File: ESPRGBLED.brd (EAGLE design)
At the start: 22.5 x 25.7 mm, 25 parts

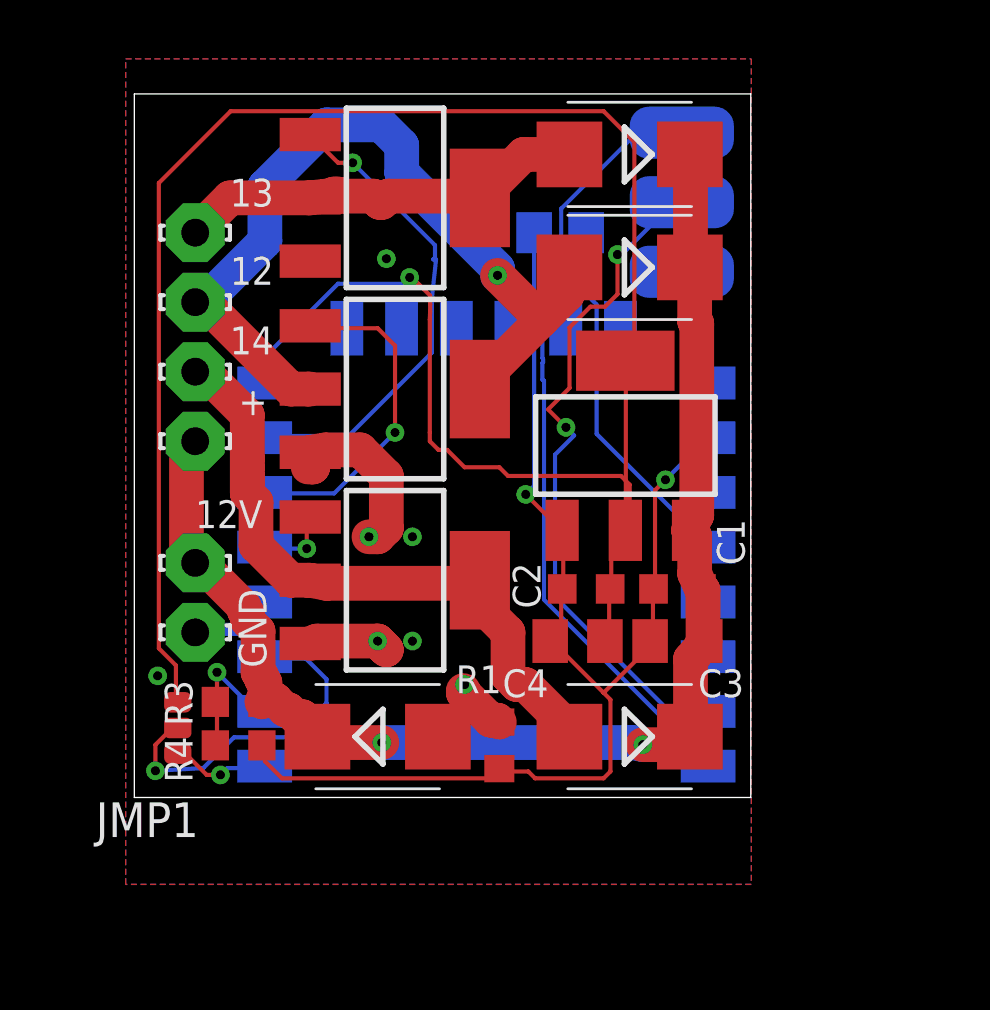
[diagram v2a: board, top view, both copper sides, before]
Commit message: updated schematics with step down vreg
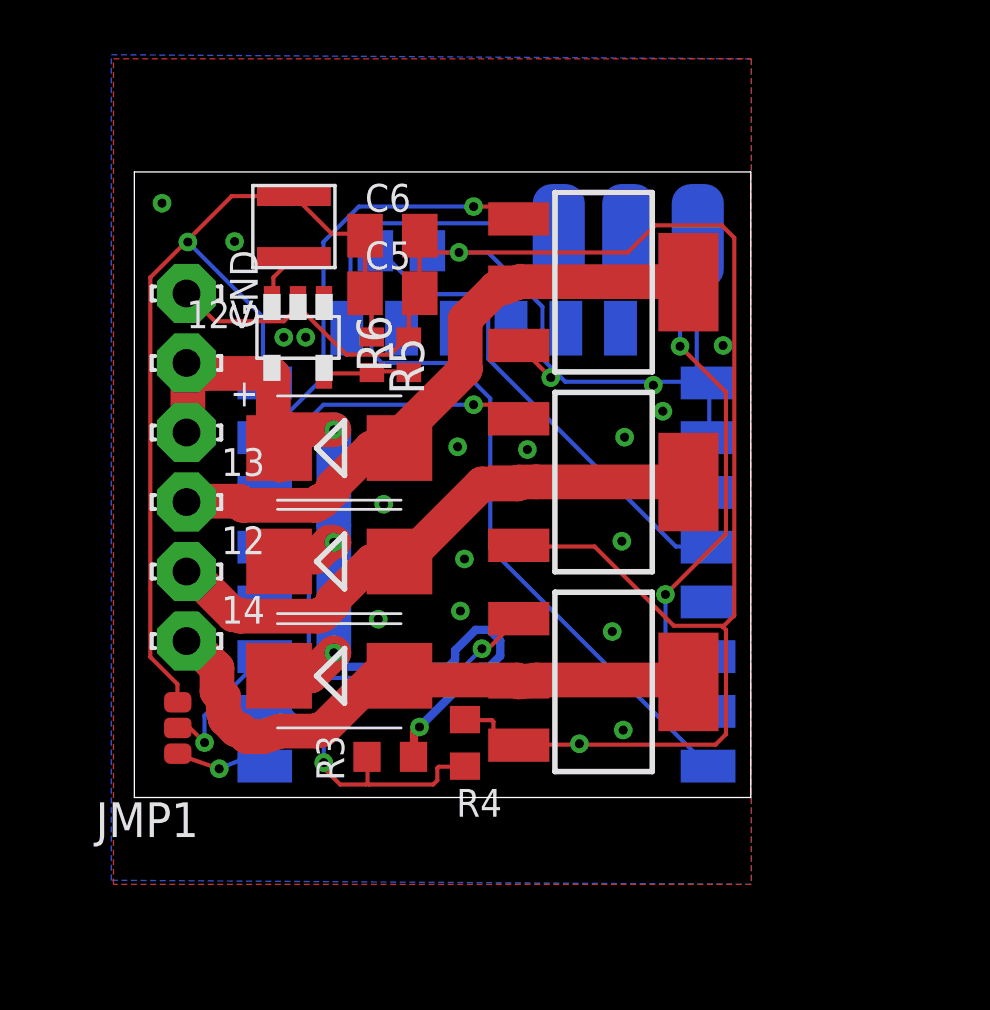
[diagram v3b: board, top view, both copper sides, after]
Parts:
- removed C1, C2: (no value), rcl:C0603K
- removed C3, C4: (no value), rcl:C0805K
- removed D1: MBRS130LT3, diode:SMB
- removed R1: 0R, rcl:R0603
- removed U$1: LM1117, Fabian:SOT223
- added C5, C6: 10uF, rcl:C0805K
- added L1: L_10UH_560MA, Fabian:TYS3010100M-10
- added R5, R6: (no value), rcl:R0402
- added U$2: TPS560200, Fabian:SOT23-5
- moved PWR2:D1 15.1 mm to (6.22, 11.8), turned to 0 degrees
- moved PWR1:D1 15.1 mm to (6.22, 15.9), turned to 0 degrees
- moved GND 12.4 mm to (0.64, 21.6)
- moved PWR3:D1 10.8 mm to (6.22, 7.62), turned to 0 degrees
- moved 12 9.85 mm to (0.64, 11.4)
- moved 14 9.85 mm to (0.64, 8.89)
- moved 13 9.85 mm to (0.64, 14.0)
- moved PWR3:T1 8.48 mm to (15.9, 7.40)
- moved PWR2:T1 8.34 mm to (15.9, 14.7)
- moved R4 8.27 mm to (10.8, 5.17), turned to 270 degrees
- moved PWR1:T1 8.22 mm to (15.9, 22.0)
- moved 12V 7.31 mm to (0.64, 19.1)
- moved R3 5.89 mm to (8.08, 4.66)
- moved R2 5.84 mm to (8.49, 23.2), turned to 180 degrees
- moved U$3 2.32 mm to (16.8, 23.7), turned to 0 degrees
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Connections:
- removed net DGND: C1.2, C2.2, C3.2, C4.2, MDL1.10, MDL1.9, R1.1, R2.2, R4.1, U$1.LEFT, U$3.0V
- new net N$13: L1.P$1, U$2.3
- new net N$15: R5.2, R6.1, U$2.5
- net +12V: now also U$2.4; no longer C1.1, C3.1, D1.C, U$1.RIGHT
- net GND: now also C5.2, C6.2, MDL1.10, MDL1.9, R2.2, R4.1, R6.2, U$2.2, U$3.0V; no longer D1.A, R1.2
- net VCC: now also C5.1, C6.1, L1.P$2, R5.1; no longer C2.1, C4.1, U$1.MID, U$1.TAP
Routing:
- net GND: track 12.9 -> 87.7 mm, vias 7 -> 20
- net DGND: track 55.5 -> 0.00 mm, vias 2 -> 0
- net VCC: track 80.4 -> 35.8 mm
- net +12V: track 49.1 -> 37.5 mm, vias 2 -> 4
- net N$2: track 2.80 -> 13.7 mm
- net N$4: track 31.6 -> 21.1 mm, vias 1 -> 0
- net N$1: track 15.1 -> 23.2 mm
- net N$12: track 12.8 -> 5.27 mm
- net N$10: track 5.07 -> 10.5 mm
- net N$8: track 25.8 -> 20.4 mm
- net N$7: track 29.3 -> 34.5 mm
- net N$9: track 13.4 -> 17.8 mm
- net N$15: track 0.00 -> 3.16 mm
- net N$5: track 23.9 -> 21.8 mm
- net N$13: track 0.00 -> 1.93 mm
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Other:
- board size 22.5 x 25.7 mm -> 22.5 x 22.9 mm

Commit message: layout stuff
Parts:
- moved JMP1 23.2 mm to (23.2, 2.02), turned to 270 degrees
- moved C6 20.6 mm to (11.0, 3.27), turned to 270 degrees
- moved MDL1 18.8 mm to (8.17, 2.12), turned to 90 degrees
- moved L1 18.5 mm to (11.3, 6.87), turned to 0 degrees
- moved C5 18.3 mm to (8.90, 3.27), turned to 270 degrees
- moved R6 16.5 mm to (6.70, 3.02), turned to 0 degrees
- moved GND 15.3 mm to (1.91, 6.35)
- moved R5 15.0 mm to (6.70, 4.32), turned to 180 degrees
- moved U$2 13.5 mm to (7.29, 6.72), turned to 90 degrees
- moved 12V 10.2 mm to (1.91, 8.89)
- moved R4 9.01 mm to (1.95, 3.54)
- moved PWR1:D1 5.68 mm to (8.76, 21.0)
- moved + 5.24 mm to (1.91, 11.4)
- moved 12 5.24 mm to (1.91, 16.5)
- moved 13 5.24 mm to (1.91, 19.1)
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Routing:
- net N$7: track 34.5 -> 3.56 mm
- net N$10: track 10.5 -> 32.0 mm, vias 1 -> 3
- net N$8: track 20.4 -> 3.81 mm, vias 2 -> 0
- net GND: track 87.7 -> 99.1 mm
- net +12V: track 37.5 -> 27.6 mm, vias 4 -> 2
- net N$6: track 15.9 -> 23.4 mm, vias 1 -> 3
- net N$2: track 13.7 -> 6.22 mm
- net N$5: track 21.8 -> 28.3 mm, vias 0 -> 1
- net N$9: track 17.8 -> 12.5 mm
- net VCC: track 35.8 -> 32.0 mm, vias 1 -> 2
- net N$3: track 11.5 -> 14.1 mm
- net N$4: track 21.1 -> 23.4 mm, vias 0 -> 1
- net N$15: track 3.16 -> 3.89 mm
- net N$1: track 23.2 -> 22.5 mm
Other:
- board size 22.5 x 22.9 mm -> 25.2 x 24.1 mm

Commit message: superminiaturized
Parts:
- added C1, C2: 10uF, rcl:C0805K
- added R1: 0R, rcl:R0402
- R5: value (none) -> 61k9
- R6: value (none) -> 20k
- moved U$3 25.8 mm to (4.12, 2.40), turned to 0 degrees
- moved MDL1 22.0 mm to (17.1, 22.2), turned to 270 degrees
- moved JMP1 20.6 mm to (19.1, 22.2), flipped to the bottom
- moved R2 20.5 mm to (11.0, 2.71), turned to 180 degrees
- moved C6 20.2 mm to (2.54, 21.6), turned to 0 degrees
- moved + 17.8 mm to (19.7, 11.7)
- moved 12 17.8 mm to (19.7, 16.8)
- moved 12V 17.8 mm to (19.7, 9.21)
- moved 13 17.8 mm to (19.7, 19.4)
- moved 14 17.8 mm to (19.7, 14.3)
- moved GND 17.8 mm to (19.7, 6.67)
- moved C5 17.6 mm to (2.54, 19.7), turned to 0 degrees
- moved L1 13.3 mm to (2.54, 16.8), turned to 90 degrees
- moved PWR3:T1 10.8 mm to (8.89, 5.40)
- moved PWR2:T1 10.8 mm to (8.89, 12.4)
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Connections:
- net N$10 renamed ADC
- net N$11 renamed REST
- net N$12 renamed CH_PD
- net N$2 renamed GPIO14
- net N$3 renamed GPIO12
- net N$6 renamed GPIO13
- net N$9 renamed GPIO0
- new net VIN: C1.1, C2.1, R1.2, R3.2, U$2.4
- net +12V: now also R1.1; no longer R3.2, U$2.4
- net GND: now also C1.2, C2.2
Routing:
- net GND: track 99.1 -> 59.2 mm, vias 20 -> 24
- net VIN: track 0.00 -> 21.9 mm, vias 0 -> 2
- net REST: track 3.37 -> 24.2 mm, vias 1 -> 0
- net CH_PD: track 5.60 -> 18.3 mm, vias 1 -> 2
- net GPIO14: track 6.22 -> 16.0 mm, vias 1 -> 3
- net N$5: track 28.3 -> 19.3 mm, vias 1 -> 0
- net GPIO0: track 12.5 -> 3.72 mm
- net N$4: track 23.4 -> 15.9 mm, vias 1 -> 0
- net N$1: track 22.5 -> 16.2 mm
- net ADC: track 32.0 -> 26.0 mm
- net GPIO13: track 23.4 -> 19.1 mm, vias 3 -> 1
- net GPIO12: track 14.1 -> 10.5 mm
- net VCC: track 32.0 -> 35.1 mm, vias 2 -> 3
- net +12V: track 27.6 -> 29.9 mm, vias 2 -> 3
- net N$15: track 3.89 -> 2.61 mm
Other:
- board size 25.2 x 24.1 mm -> 21.4 x 22.5 mm
